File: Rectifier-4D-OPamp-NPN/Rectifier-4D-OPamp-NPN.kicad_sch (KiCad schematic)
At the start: 16 parts, among them Q1 NPN, U1 ${SIM.PARAMS}

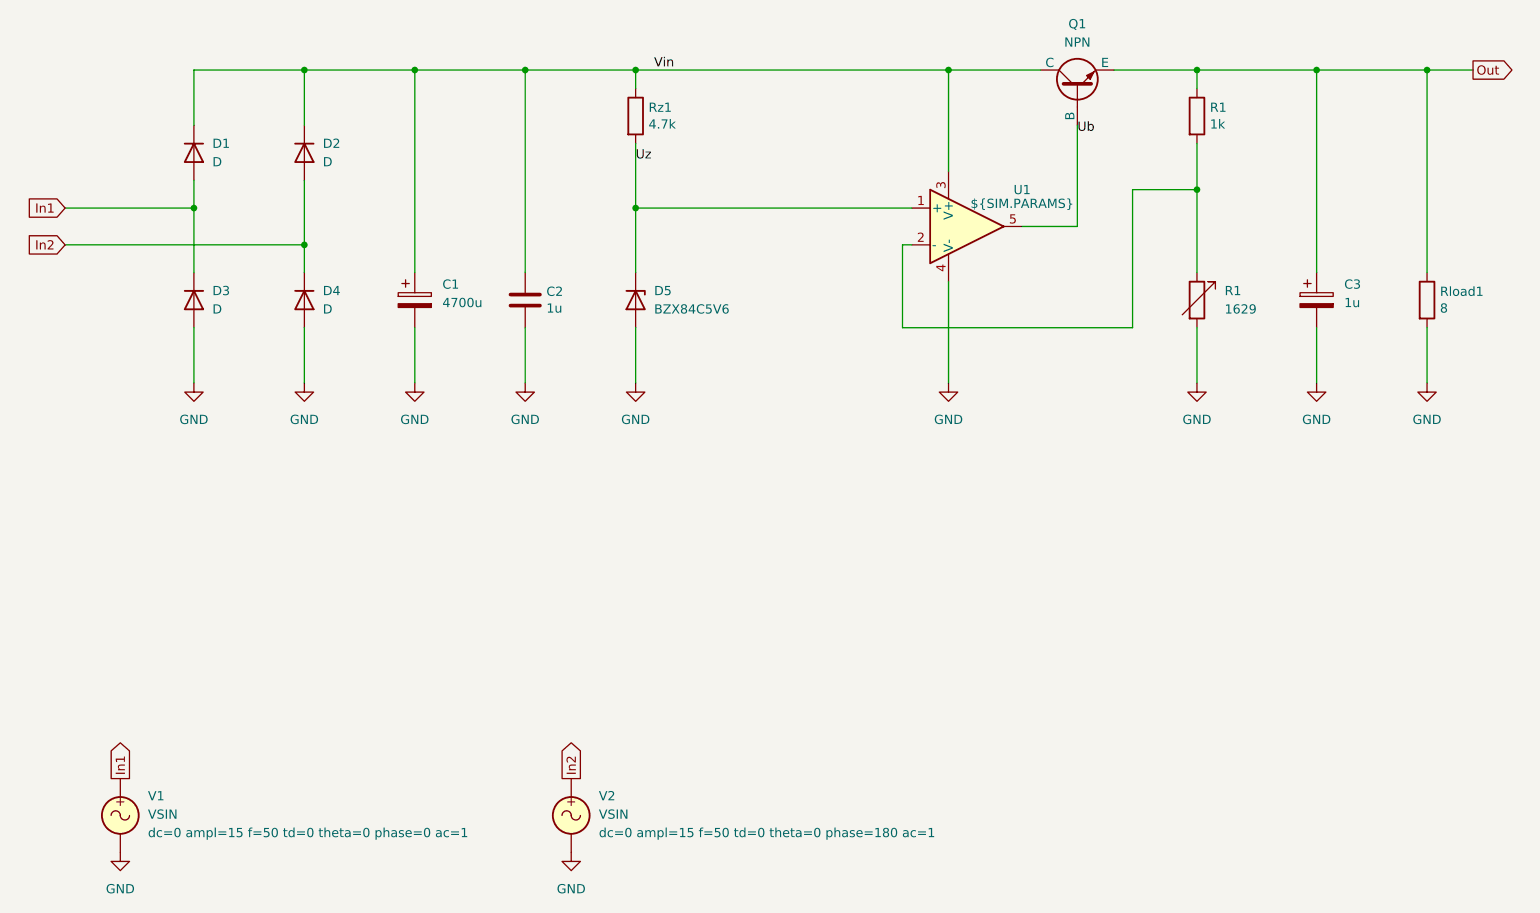
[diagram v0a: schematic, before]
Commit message: Tested/updated for KiCad 9
Schematics are tested and updated for KiCad 9, no changes in circuitry
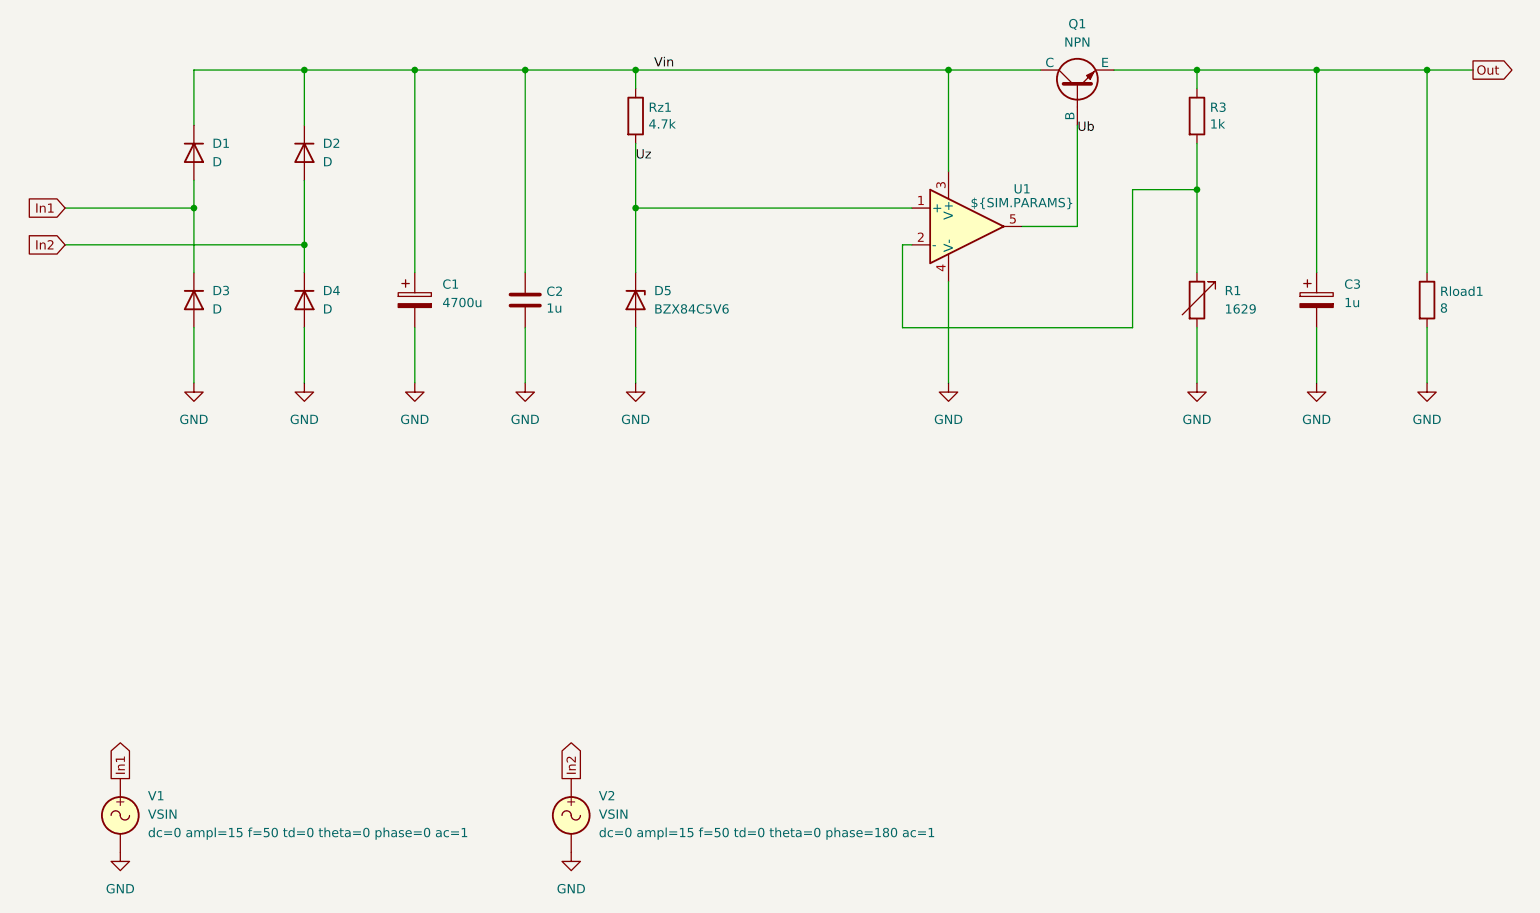
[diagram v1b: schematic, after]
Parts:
- renumbered R1 to R3
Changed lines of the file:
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@@
 (kicad_sch
-	(version 20231120)
+	(version 20250114)
 	(generator "eeschema")
-	(generator_version "8.0")
+	(generator_version "9.0")
 	(paper "A4")
 	(title_block
 		(title "Rectifier with 4 diodes, OPamp and NPN passtransistor")
-		(date "2024-12-15")
+		(date "2025-09-13")
 		(company "GitHub/OJStuff")
 	)
@@
 	(label "Ub"
 		(at 187.96 87.63 0)
-		(fields_autoplaced yes)
 		(effects
 			(font
@@
 	(label "Uz"
 		(at 127 91.44 0)
-		(fields_autoplaced yes)
 		(effects
 			(font
@@
 	(label "Vin"
 		(at 129.54 78.74 0)
-		(fields_autoplaced yes)
 		(effects
 			(font
@@
 	)
 	(symbol
+		(lib_id "Simulation_SPICE:OPAMP")
+		(at 172.72 100.33 0)
+		(unit 1)
+		(exclude_from_sim no)
+		(in_bom yes)
+		(on_board yes)
+		(dnp no)
+		(fields_autoplaced yes)
+		(property "Reference" "U1"
+			(at 180.34 95.1798 0)
+			(effects
+				(font
+					(size 1.27 1.27)
+				)
+			)
+		)
+		(property "Value" "${SIM.PARAMS}"
+			(at 180.34 97.0849 0)
+			(effects
+				(font
+					(size 1.27 1.27)
+				)
+			)
+		)
+		(property "Footprint" ""
+			(at 172.72 100.33 0)
+			(effects
+				(font
+					(size 1.27 1.27)
+				)
+				(hide yes)
+			)
+		)
+		(property "Datasheet" "https://ngspice.sourceforge.io/docs/ngspice-html-manual/manual.xhtml#sec__SUBCKT_Subcircuits"
+			(at 172.72 100.33 0)
+			(effects
+				(font
+					(size 1.27 1.27)
+				)
+				(hide yes)
+			)
+		)
+		(property "Description" "Operational amplifier, single"
+			(at 172.72 100.33 0)
+			(effects
+				(font
+					(size 1.27 1.27)
+				)
+				(hide yes)
+			)
+		)
+		(property "Sim.Pins" "1=in+ 2=in- 3=vcc 4=vee 5=out"
+			(at 172.72 100.33 0)
+			(effects
+				(font
+					(size 1.27 1.27)
+				)
+				(hide yes)
+			)
+		)
+		(property "Sim.Device" "SUBCKT"
+			(at 172.72 100.33 0)
+			(effects
+				(font
+					(size 1.27 1.27)
+				)
+				(justify left)
+				(hide yes)
+			)
+		)
+		(property "Sim.Library" "${KICAD9_SYMBOL_DIR}/Simulation_SPICE.sp"
+			(at 172.72 100.33 0)
+			(effects
+				(font
+					(size 1.27 1.27)
+				)
+				(hide yes)
+			)
+		)
+		(property "Sim.Name" "kicad_builtin_opamp"
+			(at 172.72 100.33 0)
+			(effects
+				(font
+					(size 1.27 1.27)
+				)
+				(hide yes)
+			)
+		)
+		(pin "5"
+		)
+		(pin "3"
+		)
+		(pin "4"
+		)
+		(pin "2"
+		)
+		(pin "1"
+		)
+		(instances
+			(project ""
+				(path "/95246ab0-aedc-41ad-8fc8-1776512f8fe1"
+					(reference "U1")
+					(unit 1)
+				)
+			)
+		)
+	)
+	(symbol
 		(lib_name "GND_1")
 		(lib_id "power:GND")
@@
 		(on_board yes)
 		(dnp no)
-		(property "Reference" "R1"
+		(property "Reference" "R3"
 			(at 206.248 83.9216 0)
 			(effects
@@
 				(path "/95246ab0-aedc-41ad-8fc8-1776512f8fe1"
 					(reference "R3")
-					(unit 1)
-				)
-			)
-		)
-	)
-	(symbol
-		(lib_id "Simulation_SPICE:OPAMP")
-		(at 172.72 100.33 0)
-		(unit 1)
-		(exclude_from_sim no)
-		(in_bom yes)
-		(on_board yes)
-		(dnp no)
-		(fields_autoplaced yes)
-		(property "Reference" "U1"
-			(at 180.34 95.2814 0)
-			(effects
-				(font
-					(size 1.27 1.27)
-				)
-			)
-		)
-		(property "Value" "${SIM.PARAMS}"
-			(at 180.34 97.1865 0)
-			(effects
-				(font
-					(size 1.27 1.27)
-				)
-			)
-		)
-		(property "Footprint" ""
-			(at 172.72 100.33 0)
-			(effects
-				(font
-					(size 1.27 1.27)
-				)
-				(hide yes)
-			)
-		)
-		(property "Datasheet" "https://ngspice.sourceforge.io/docs/ngspice-html-manual/manual.xhtml#sec__SUBCKT_Subcircuits"
-			(at 172.72 100.33 0)
-			(effects
-				(font
-					(size 1.27 1.27)
-				)
-				(hide yes)
-			)
-		)
-		(property "Description" "Operational amplifier, single, node sequence=1:+ 2:- 3:OUT 4:V+ 5:V-"
-			(at 172.72 100.33 0)
-			(effects
-				(font
-					(size 1.27 1.27)
-				)
-				(hide yes)
-			)
-		)
-		(property "Sim.Pins" "1=in+ 2=in- 3=vcc 4=vee 5=out"
-			(at 172.72 100.33 0)
-			(effects
-				(font
-					(size 1.27 1.27)
-				)
-				(hide yes)
-			)
-		)
-		(property "Sim.Device" "SUBCKT"
-			(at 172.72 100.33 0)
-			(effects
-				(font
-					(size 1.27 1.27)
-				)
-				(justify left)
-				(hide yes)
-			)
-		)
-		(property "Sim.Library" "${KICAD7_SYMBOL_DIR}/Simulation_SPICE.sp"
-			(at 172.72 100.33 0)
-			(effects
-				(font
-					(size 1.27 1.27)
-				)
-				(hide yes)
-			)
-		)
-		(property "Sim.Name" "kicad_builtin_opamp"
-			(at 172.72 100.33 0)
-			(effects
-				(font
-					(size 1.27 1.27)
-				)
-				(hide yes)
-			)
-		)
-		(pin "2"
-		)
-		(pin "5"
-		)
-		(pin "4"
-		)
-		(pin "3"
-		)
-		(pin "1"
-		)
-		(instances
-			(project "Rectifier-4D-OPamp-NPN-(.tran)"
-				(path "/95246ab0-aedc-41ad-8fc8-1776512f8fe1"
-					(reference "U1")
 					(unit 1)
 				)
@@
 		)
 	)
+	(embedded_fonts no)
 )
